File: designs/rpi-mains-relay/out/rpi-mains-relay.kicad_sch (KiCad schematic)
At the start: 0 parts

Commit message: designs: work-in-progress (Prius encoding and relay-board rework under way)
Co-Authored-By: Claude Opus 5.5 <noreply@anthropic.com>
Claude-Session: https://claude.ai/code/session_01VFJn9VbX8h27kf4LpLwEtn
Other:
- removed sheet selv_in
- added sheet ch5 (ch5.kicad_sch)
- added sheet ch6 (ch6.kicad_sch)
- added sheet outlets (outlets.kicad_sch)
- added sheet pi (pi.kicad_sch)
- added sheet power5 (power5.kicad_sch)
- note added: "5 V rail: bulk caps, TVS, PWR LED, Pi branch PTC"
- note added: "Heartbeat watchdog U1, arming switch Q7 and readback"
- note added: "Holes; partition; enclosures, receptacles, Pi and hardware (BOM only)"
- note added: "Mains input J1, supply fuse F1 and IRM-20-5"
- note added: "Outlet 1: relay K1, driver Q1"
- note added: "Outlet 2: relay K2, driver Q2"
- note added: "Outlet 3: relay K3, driver Q3"
- note added: "Outlet 4: relay K4, driver Q4"
- note added: "Outlet 5: relay K5, driver Q5"
- note added: "Outlet 6: relay K6, driver Q6"
- note added: "RPi Zero 2 W six-outlet 120 VAC relay board (polycarbonate enclosure) (rev A) Domains: LINE (mains, 0 V = L_IN); NEUTRAL (mains, 0 V = L_IN); OUT1 (mains, 0 V = L_IN); OUT2 (mains, 0 V = L_IN); OUT3 (mains, 0 V = L_IN); OUT4 (mains, 0 V = L_IN); OUT5 (mains, 0 V = L_IN); OUT6 (mains, 0 V = L_IN); PE (other, 0 V = PE); SELV (selv, 0 V = GND) Barrier SELV/LINE: reinforced, 187 V working, creepage 8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"
- note added: "Raspberry Pi Zero 2 W socket J5 (Pi component side up)"
- note added: "Receptacle feeds J2-J4 (one 14/3 NM-B cable per duplex receptacle)"
- note removed: "Channel 1: relay K1, driver Q1, output J2"
- note removed: "Channel 2: relay K2, driver Q2, output J3"
- note removed: "Channel 3: relay K3, driver Q3, output J4"
- note removed: "Channel 4: relay K4, driver Q4, output J5"
- note removed: "Class 2 link from the Pi: terminal, PTC, TVS, ESD"
- note removed: "Heartbeat watchdog (charge pump) and common coil enable"
- note removed: "Mains input terminal (shared L, N)"
- note removed: "Mounting holes, SELV cover and box parts (BOM only)"
- note removed: "RPi 4-channel 120 VAC relay board (4-11/16 in box) (rev A) Domains: LINE (mains, 0 V = L_IN); NEUTRAL (mains, 0 V = L_IN); OUT1 (mains, 0 V = L_IN); OUT2 (mains, 0 V = L_IN); OUT3 (mains, 0 V = L_IN); OUT4 (mains, 0 V = L_IN); PE (other, 0 V = PE); SELV (selv, 0 V = GND) Barrier SELV/LINE: reinforced, 187 V working, creepage 8 mm, clearance 8 mm (UL/IEC 62368-1 Tables 10 and 17; IEC 60664-1 Table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"
- title: RPi 4-channel 120 VAC relay board (4-11/16 in box) -> RPi Zero 2 W six-outlet 120 VAC relay board (polycarbonate enclosure)

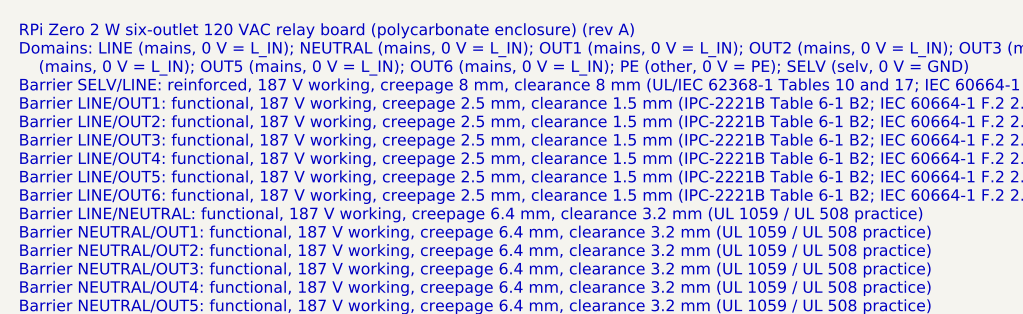
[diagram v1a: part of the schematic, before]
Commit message: designs/rpi-mains-relay: work-in-progress rework (6 receptacles, Pi Zero 2 W inside)
Co-Authored-By: Claude Opus 5.5 <noreply@anthropic.com>
Claude-Session: https://claude.ai/code/session_01VFJn9VbX8h27kf4LpLwEtn
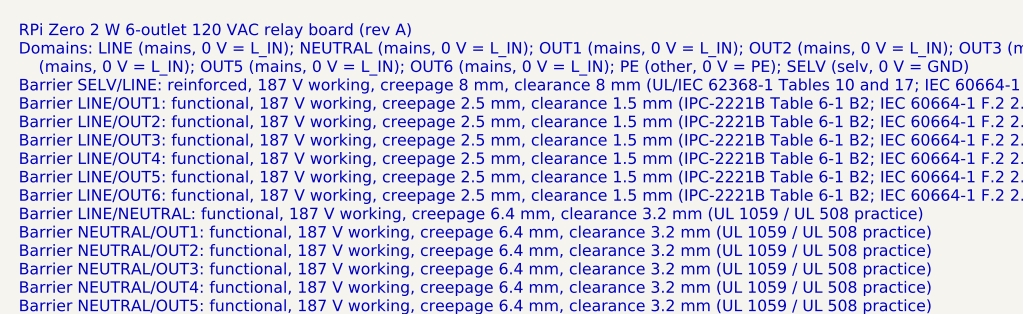
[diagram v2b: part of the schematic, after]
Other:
- note added: "RPi Zero 2 W 6-outlet 120 VAC relay board (rev A) Domains: LINE (mains, 0 V = L_IN); NEUTRAL (mains, 0 V = L_IN); OUT1 (mains, 0 V = L_IN); OUT2 (mains, 0 V = L_IN); OUT3 (mains, 0 V = L_IN); OUT4 (mains, 0 V = L_IN); OUT5 (mains, 0 V = L_IN); OUT6 (mains, 0 V = L_IN); PE (other, 0 V = PE); SELV (selv, 0 V = GND) Barrier SELV/LINE: reinforced, 187 V working, creepage 8 mm, clearance 8 mm (UL/IEC 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"
- note removed: "RPi Zero 2 W six-outlet 120 VAC relay board (polycarbonate enclosure) (rev A) Domains: LINE (mains, 0 V = L_IN); NEUTRAL (mains, 0 V = L_IN); OUT1 (mains, 0 V = L_IN); OUT2 (mains, 0 V = L_IN); OUT3 (mains, 0 V = L_IN); OUT4 (mains, 0 V = L_IN); OUT5 (mains, 0 V = L_IN); OUT6 (mains, 0 V = L_IN); PE (other, 0 V = PE); SELV (selv, 0 V = GND) Barrier SELV/LINE: reinforced, 187 V working, creepage 8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"
- title: RPi Zero 2 W six-outlet 120 VAC relay board (polycarbonate enclosure) -> RPi Zero 2 W 6-outlet 120 VAC relay board
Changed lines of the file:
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@@
 	(paper "A3")
 	(title_block
-		(title "RPi Zero 2 W six-outlet 120 VAC relay board (polycarbonate enclosure)")
+		(title "RPi Zero 2 W 6-outlet 120 VAC relay board")
 		(date "2026-10-23")
 		(rev "A")
 		(company "kaesynth")
-		(comment 1 "6 x 16 A relays switch line to 3 split-tab TR duplex receptacles; on-board Pi Zero 2 W fed by a Mean Well IRM-20-5; heartbeat watchdog")
+		(comment 1 "6 relays switch line to 3 split-tab TR duplexes; Pi Zero 2 W on J5; IRM-20-5 supply")
 	)
 	(sheet
@@
 		)
 	)
-	(text "RPi Zero 2 W six-outlet 120 VAC relay board (polycarbonate enclosure) (rev A)\nDomains: LINE (mains, 0 V = L_IN); NEUTRAL (mains, 0 V = L_IN); OUT1 (mains, 0 V = L_IN); OUT2 (mains, 0 V = L_IN); OUT3 (mains, 0 V = L_IN); OUT4\n    (mains, 0 V = L_IN); OUT5 (mains, 0 V = L_IN); OUT6 (mains, 0 V = L_IN); PE (other, 0 V = PE); SELV (selv, 0 V = GND)\nBarrier SELV/LINE: reinforced, 187 V working, creepage 8 mm, clearance 8 mm (UL/IEC 62368-1 Tables 10 and 17; IEC 60664-1 Tables F.1, F.2, F.4)\nBarrier LINE/OUT1: functional, 187 V working, creepage 2.5 mm, clearance 1.5 mm (IPC-2221B Table 6-1 B2; IEC 60664-1 F.2 2.5 kV)\nBarrier LINE/OUT2: functional, 187 V working, creepage 2.5 mm, clearance 1.5 mm (IPC-2221B Table 6-1 B2; IEC 60664-1 F.2 2.5 kV)\nBarrier LINE/OUT3: functional, 187 V working, creepage 2.5 mm, clearance 1.5 mm (IPC-2221B Table 6-1 B2; IEC 60664-1 F.2 2.5 kV)\nBarrier LINE/OUT4: functional, 187 V working, creepage 2.5 mm, clearance 1.5 mm (IPC-2221B Table 6-1 B2; IEC 60664-1 F.2 2.5 kV)\nBarrier LINE/OUT5: functional, 187 V working, creepage 2.5 mm, clearance 1.5 mm (IPC-2221B Table 6-1 B2; IEC 60664-1 F.2 2.5 kV)\nBarrier LINE/OUT6: functional, 187 V working, creepage 2.5 mm, clearance 1.5 mm (IPC-2221B Table 6-1 B2; IEC 60664-1 F.2 2.5 kV)\nBarrier LINE/NEUTRAL: functional, 187 V working, creepage 6.4 mm, clearance 3.2 mm (UL 1059 / UL 508 practice)\nBarrier NEUTRAL/OUT1: functional, 187 V working, creepage 6.4 mm, clearance 3.2 mm (UL 1059 / UL 508 practice)\nBarrier NEUTRAL/OUT2: functional, 187 V working, creepage 6.4 mm, clearance 3.2 mm (UL 1059 / UL 508 practice)\nBarrier NEUTRAL/OUT3: functional, 187 V working, creepage 6.4 mm, clearance 3.2 mm (UL 1059 / UL 508 practice)\nBarrier NEUTRAL/OUT4: functional, 187 V working, creepage 6.4 mm, clearance 3.2 mm (UL 1059 / UL 508 practice)\nBarrier NEUTRAL/OUT5: functional, 187 V working, creepage 6.4 mm, clearance 3.2 mm (UL 1059 / UL 508 practice)\nBarrier NEUTRAL/OUT6: functional, 187 V working, creepage 6.4 mm, clearance 3.2 mm (UL 1059 / UL 508 practice)\nBarrier OUT1/OUT2: functional, 187 V working, creepage 6.4 mm, clearance 3.2 mm (UL 1059 / UL 508 practice)\nBarrier OUT1/OUT3: functional, 187 V working, creepage 6.4 mm, clearance 3.2 mm (UL 1059 / UL 508 practice)\nBarrier OUT1/OUT4: functional, 187 V working, creepage 6.4 mm, clearance 3.2 mm (UL 1059 / UL 508 practice)\nBarrier OUT1/OUT5: functional, 187 V working, creepage 6.4 mm, clearance 3.2 mm (UL 1059 / UL 508 practice)\nBarrier OUT1/OUT6: functional, 187 V working, creepage 6.4 mm, clearance 3.2 mm (UL 1059 / UL 508 practice)\nBarrier OUT2/OUT3: functional, 187 V working, creepage 6.4 mm, clearance 3.2 mm (UL 1059 / UL 508 practice)\nBarrier OUT2/OUT4: functional, 187 V working, creepage 6.4 mm, clearance 3.2 mm (UL 1059 / UL 508 practice)\nBarrier OUT2/OUT5: functional, 187 V working, creepage 6.4 mm, clearance 3.2 mm (UL 1059 / UL 508 practice)\nBarrier OUT2/OUT6: functional, 187 V working, creepage 6.4 mm, clearance 3.2 mm (UL 1059 / UL 508 practice)\nBarrier OUT3/OUT4: functional, 187 V working, creepage 6.4 mm, clearance 3.2 mm (UL 1059 / UL 508 practice)\nBarrier OUT3/OUT5: functional, 187 V working, creepage 6.4 mm, clearance 3.2 mm (UL 1059 / UL 508 practice)\nBarrier OUT3/OUT6: functional, 187 V working, creepage 6.4 mm, clearance 3.2 mm (UL 1059 / UL 508 practice)\nBarrier OUT4/OUT5: functional, 187 V working, creepage 6.4 mm, clearance 3.2 mm (UL 1059 / UL 508 practice)\nBarrier OUT4/OUT6: functional, 187 V working, creepage 6.4 mm, clearance 3.2 mm (UL 1059 / UL 508 practice)\nBarrier OUT5/OUT6: functional, 187 V working, creepage 6.4 mm, clearance 3.2 mm (UL 1059 / UL 508 practice)\nBarrier LINE/PE: basic, 187 V working, creepage 6.4 mm, clearance 6.4 mm (IEC 62368-1 basic; UL field wiring to dead metal)\nNOT READY FOR FABRICATION — blocking questions: Q-1, Q-6, Q-7, Q-8"
+	(text "RPi Zero 2 W 6-outlet 120 VAC relay board (rev A)\nDomains: LINE (mains, 0 V = L_IN); NEUTRAL (mains, 0 V = L_IN); OUT1 (mains, 0 V = L_IN); OUT2 (mains, 0 V = L_IN); OUT3 (mains, 0 V = L_IN); OUT4\n    (mains, 0 V = L_IN); OUT5 (mains, 0 V = L_IN); OUT6 (mains, 0 V = L_IN); PE (other, 0 V = PE); SELV (selv, 0 V = GND)\nBarrier SELV/LINE: reinforced, 187 V working, creepage 8 mm, clearance 8 mm (UL/IEC 62368-1 Tables 10 and 17; IEC 60664-1 Tables F.1, F.2, F.4)\nBarrier LINE/OUT1: functional, 187 V working, creepage 2.5 mm, clearance 1.5 mm (IPC-2221B Table 6-1 B2; IEC 60664-1 F.2 2.5 kV)\nBarrier LINE/OUT2: functional, 187 V working, creepage 2.5 mm, clearance 1.5 mm (IPC-2221B Table 6-1 B2; IEC 60664-1 F.2 2.5 kV)\nBarrier LINE/OUT3: functional, 187 V working, creepage 2.5 mm, clearance 1.5 mm (IPC-2221B Table 6-1 B2; IEC 60664-1 F.2 2.5 kV)\nBarrier LINE/OUT4: functional, 187 V working, creepage 2.5 mm, clearance 1.5 mm (IPC-2221B Table 6-1 B2; IEC 60664-1 F.2 2.5 kV)\nBarrier LINE/OUT5: functional, 187 V working, creepage 2.5 mm, clearance 1.5 mm (IPC-2221B Table 6-1 B2; IEC 60664-1 F.2 2.5 kV)\nBarrier LINE/OUT6: functional, 187 V working, creepage 2.5 mm, clearance 1.5 mm (IPC-2221B Table 6-1 B2; IEC 60664-1 F.2 2.5 kV)\nBarrier LINE/NEUTRAL: functional, 187 V working, creepage 6.4 mm, clearance 3.2 mm (UL 1059 / UL 508 practice)\nBarrier NEUTRAL/OUT1: functional, 187 V working, creepage 6.4 mm, clearance 3.2 mm (UL 1059 / UL 508 practice)\nBarrier NEUTRAL/OUT2: functional, 187 V working, creepage 6.4 mm, clearance 3.2 mm (UL 1059 / UL 508 practice)\nBarrier NEUTRAL/OUT3: functional, 187 V working, creepage 6.4 mm, clearance 3.2 mm (UL 1059 / UL 508 practice)\nBarrier NEUTRAL/OUT4: functional, 187 V working, creepage 6.4 mm, clearance 3.2 mm (UL 1059 / UL 508 practice)\nBarrier NEUTRAL/OUT5: functional, 187 V working, creepage 6.4 mm, clearance 3.2 mm (UL 1059 / UL 508 practice)\nBarrier NEUTRAL/OUT6: functional, 187 V working, creepage 6.4 mm, clearance 3.2 mm (UL 1059 / UL 508 practice)\nBarrier OUT1/OUT2: functional, 187 V working, creepage 6.4 mm, clearance 3.2 mm (UL 1059 / UL 508 practice)\nBarrier OUT1/OUT3: functional, 187 V working, creepage 6.4 mm, clearance 3.2 mm (UL 1059 / UL 508 practice)\nBarrier OUT1/OUT4: functional, 187 V working, creepage 6.4 mm, clearance 3.2 mm (UL 1059 / UL 508 practice)\nBarrier OUT1/OUT5: functional, 187 V working, creepage 6.4 mm, clearance 3.2 mm (UL 1059 / UL 508 practice)\nBarrier OUT1/OUT6: functional, 187 V working, creepage 6.4 mm, clearance 3.2 mm (UL 1059 / UL 508 practice)\nBarrier OUT2/OUT3: functional, 187 V working, creepage 6.4 mm, clearance 3.2 mm (UL 1059 / UL 508 practice)\nBarrier OUT2/OUT4: functional, 187 V working, creepage 6.4 mm, clearance 3.2 mm (UL 1059 / UL 508 practice)\nBarrier OUT2/OUT5: functional, 187 V working, creepage 6.4 mm, clearance 3.2 mm (UL 1059 / UL 508 practice)\nBarrier OUT2/OUT6: functional, 187 V working, creepage 6.4 mm, clearance 3.2 mm (UL 1059 / UL 508 practice)\nBarrier OUT3/OUT4: functional, 187 V working, creepage 6.4 mm, clearance 3.2 mm (UL 1059 / UL 508 practice)\nBarrier OUT3/OUT5: functional, 187 V working, creepage 6.4 mm, clearance 3.2 mm (UL 1059 / UL 508 practice)\nBarrier OUT3/OUT6: functional, 187 V working, creepage 6.4 mm, clearance 3.2 mm (UL 1059 / UL 508 practice)\nBarrier OUT4/OUT5: functional, 187 V working, creepage 6.4 mm, clearance 3.2 mm (UL 1059 / UL 508 practice)\nBarrier OUT4/OUT6: functional, 187 V working, creepage 6.4 mm, clearance 3.2 mm (UL 1059 / UL 508 practice)\nBarrier OUT5/OUT6: functional, 187 V working, creepage 6.4 mm, clearance 3.2 mm (UL 1059 / UL 508 practice)\nBarrier LINE/PE: basic, 187 V working, creepage 6.4 mm, clearance 6.4 mm (IEC 62368-1 basic; UL field wiring to dead metal)\nNOT READY FOR FABRICATION — blocking questions: Q-1, Q-6, Q-7, Q-8"
 		(exclude_from_sim no)
 		(at 25.4 25.4 0)
